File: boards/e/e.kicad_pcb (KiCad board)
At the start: 2 copper layers, 156.8 x 170.7 mm, 24 parts, among them J1 CONN_01X02, J2 CONN_01X02, J3 CONN_01X02, U1 APA102C_x6, U10 APA102C_x2, U11 APA102C_x2, U12 APA102C_x2, U13 APA102C_x2, U14 APA102C_x3, U15 APA102C_x3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

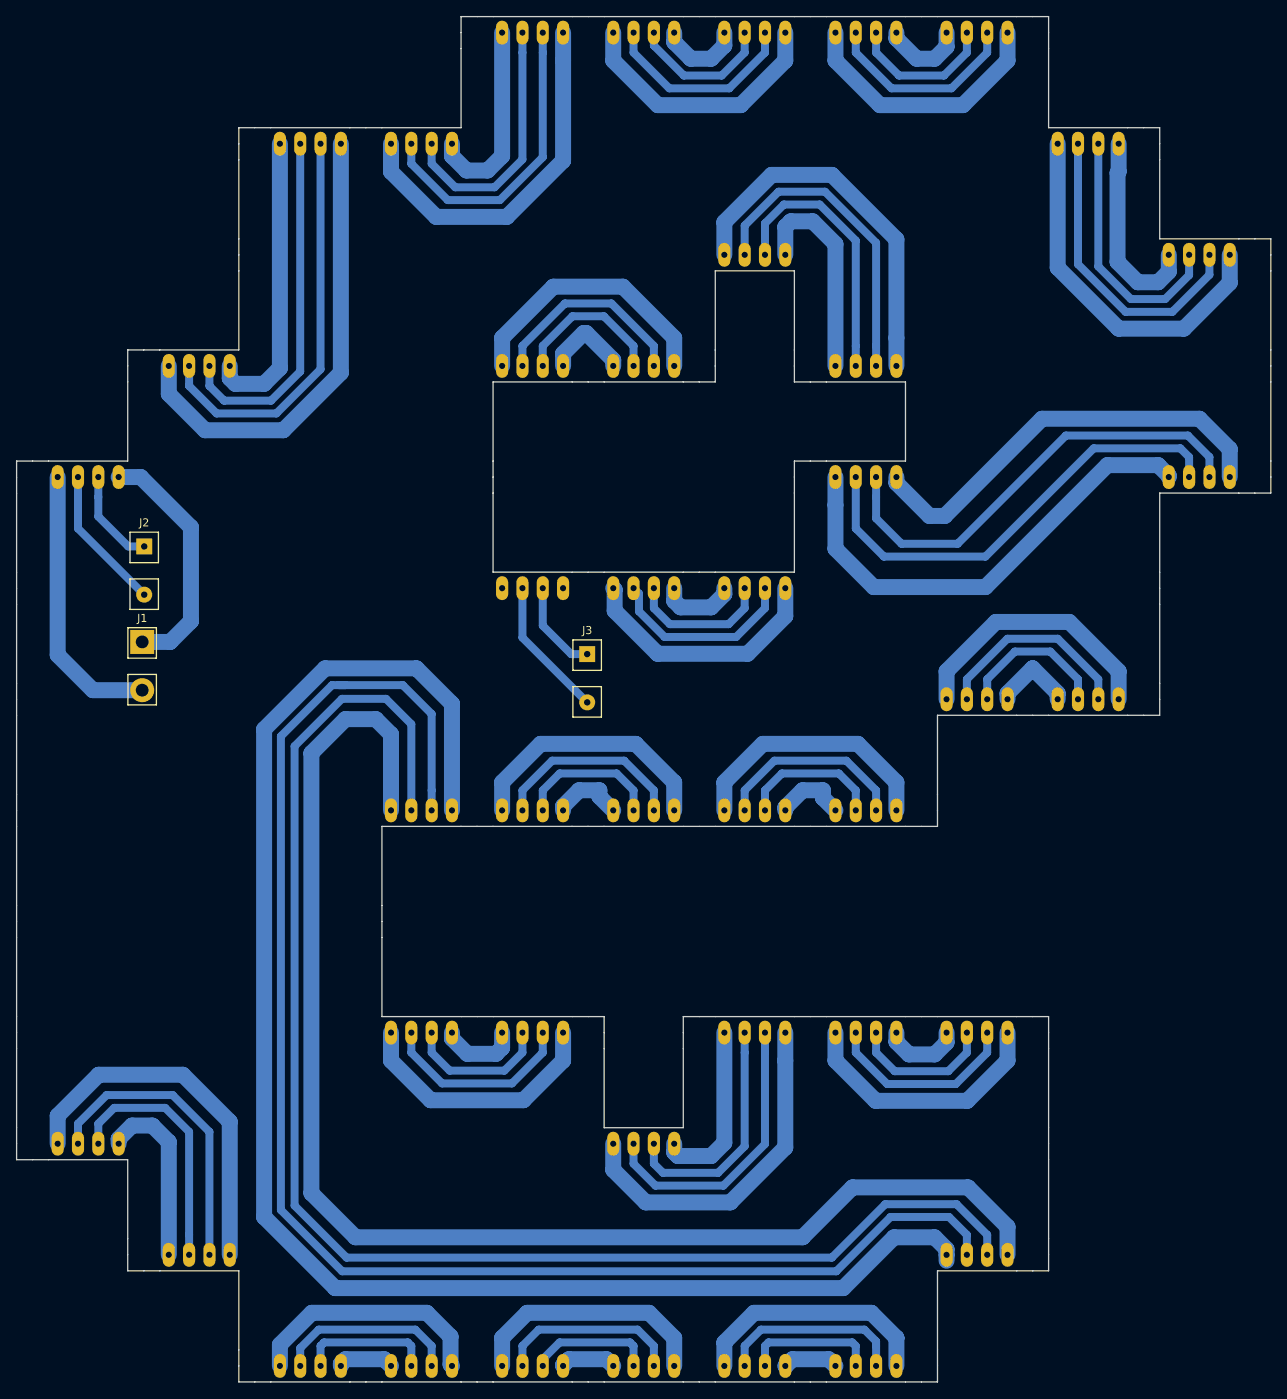
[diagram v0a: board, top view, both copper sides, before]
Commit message: Generate gerbers for all letters. Use a single drill size.
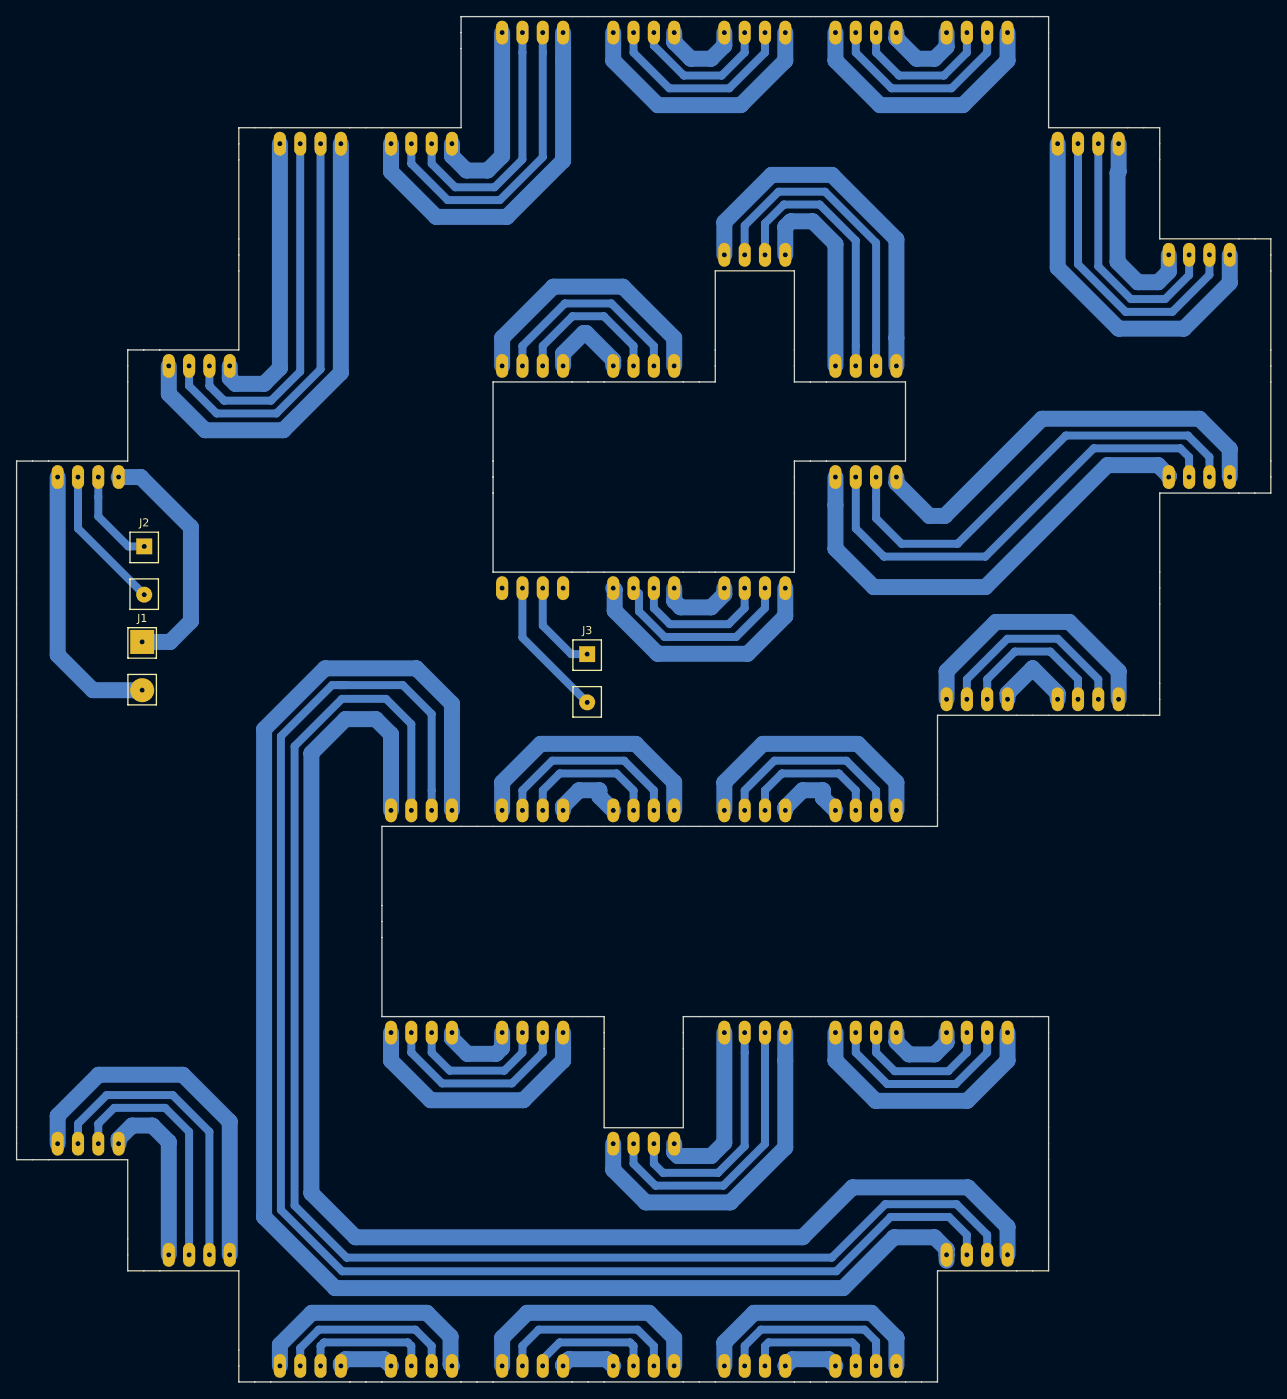
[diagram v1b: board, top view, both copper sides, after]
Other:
- net class Default: via_dia 0.6 -> None; via_drill 0.4 -> 1
- net class Signal: via_dia 0.6 -> None; via_drill 0.4 -> 1

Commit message: Boards made! Start implementing controller.
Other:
- net class Default: via_dia None -> 0.6; via_drill 1 -> 0.6
- net class Signal: via_dia None -> 0.6; via_drill 1 -> 0.6
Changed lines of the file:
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@@
   (general
     (links 86)
-    (no_connects 2)
-    (area 27.407199 47.997199 184.335001 218.813901)
+    (no_connects 0)
+    (area 27.407199 47.9722 184.335001 218.8389)
     (thickness 1.6)
     (drawings 222)
@@
       (padsonsilk false)
       (subtractmaskfromsilk false)
-      (outputformat 1)
+      (outputformat 3)
       (mirror false)
       (drillshape 0)
@@
     (clearance 0.6)
     (trace_width 2)
-    (via_drill 1)
+    (via_dia 0.6)
     (via_drill 0.6)
     (uvia_dia 0.3)
@@
     (clearance 0.6)
     (trace_width 1)
-    (via_drill 1)
+    (via_dia 0.6)
     (via_drill 0.6)
     (uvia_dia 0.3)
